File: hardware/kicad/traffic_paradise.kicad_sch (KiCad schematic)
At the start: 70 parts, among them J2 USB C, Q1 SS8050, Q2 SS8050, SW1 SW_Push, SW2 SW_Push, SW3 SW_Push, U1 ESP32-WROOM-32, U10 SN74LVC1G14DBVR, U11 SN74AHC125PWR, U2 AMS1117-3.3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

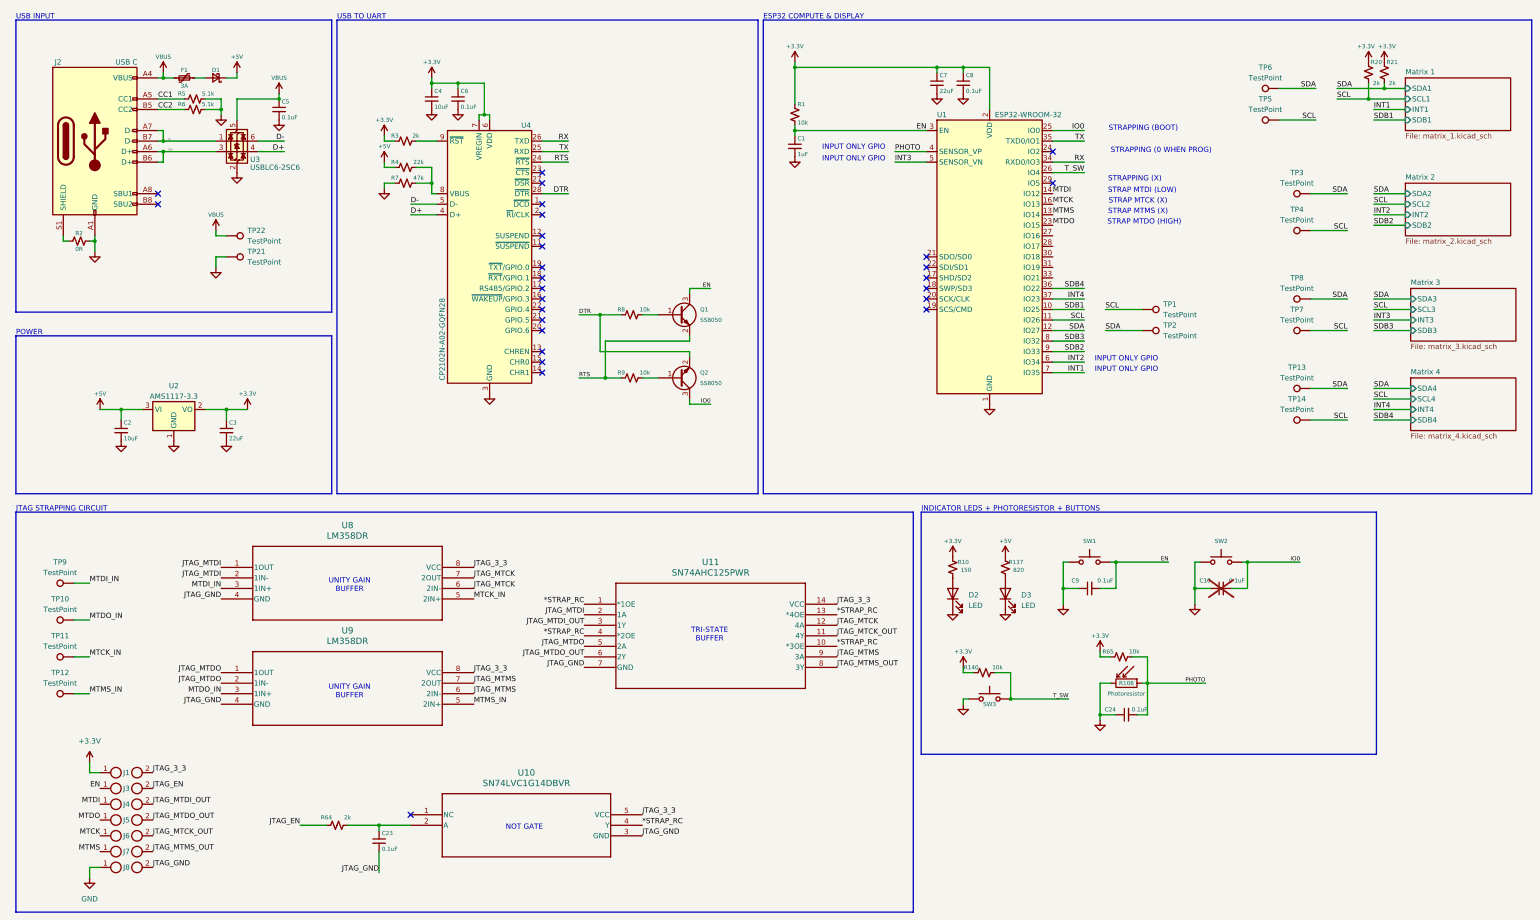
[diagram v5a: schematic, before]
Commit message: esp32c3 upgrade, route usb, fix errors
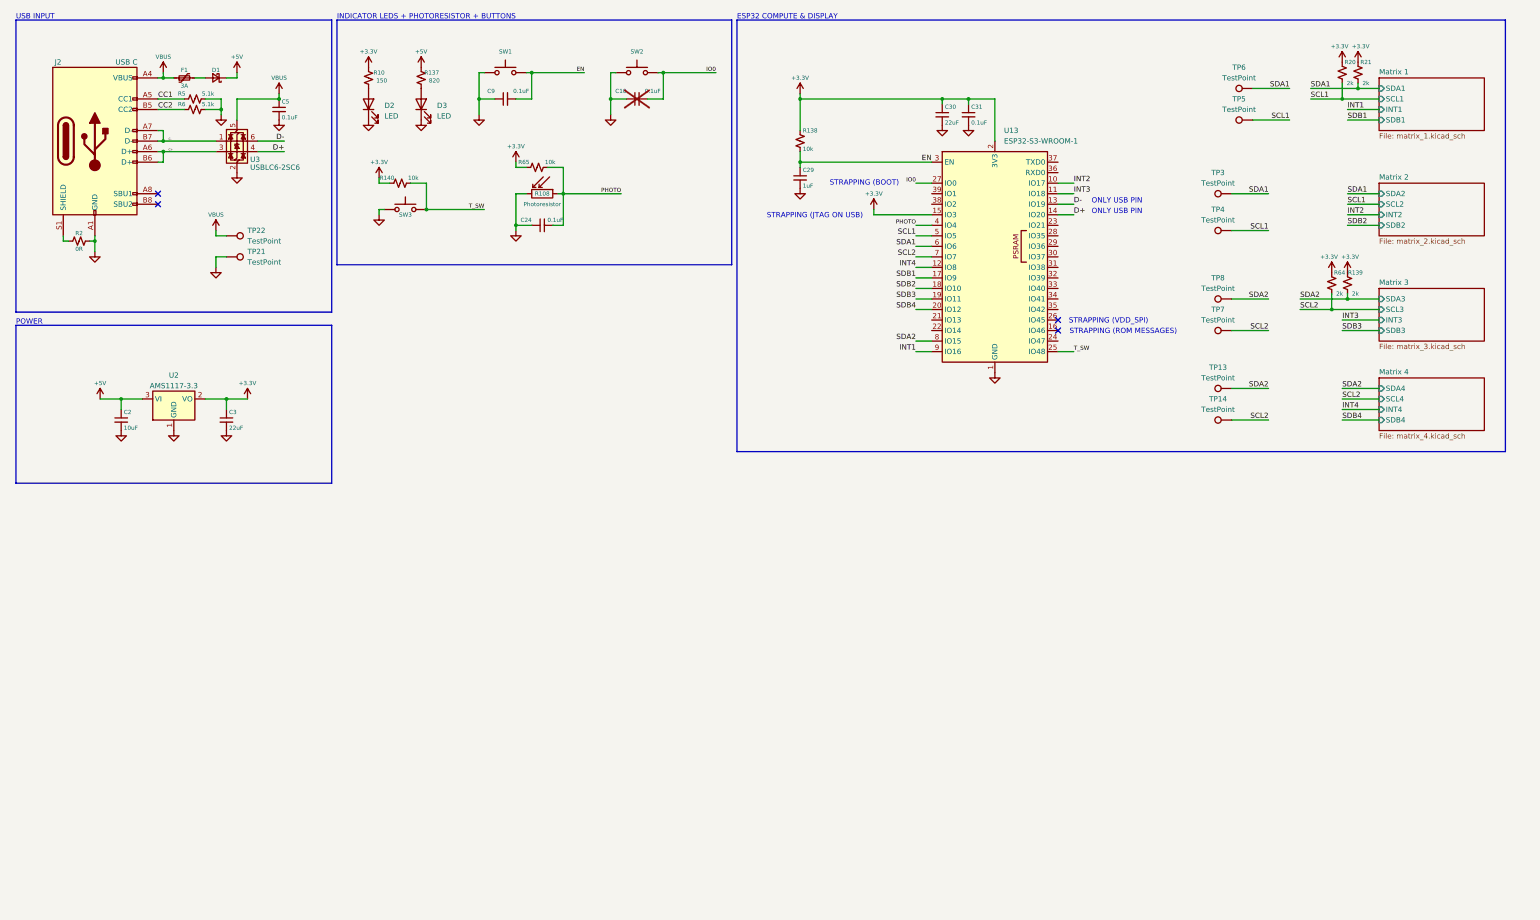
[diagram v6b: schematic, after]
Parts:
- removed C1: 1uF, Capacitor_SMD:C_0402_1005Metric, symbol Device:C_Small
- removed C23, C6, C8: 0.1uF, Capacitor_SMD:C_0402_1005Metric, symbol Device:C_Small
- removed C4: 10uF, Capacitor_SMD:C_0402_1005Metric, symbol Device:C_Small
- removed C7: 22uF, Capacitor_SMD:C_0603_1608Metric, symbol Device:C_Small
- removed J1, J3, J4, J5, J6, J7, J8: ~, Jumper:SolderJumper-2_P1.3mm_Open_TrianglePad1.0x1.5mm, symbol Isolators:breadboard_jumper
- removed Q1, Q2: SS8050, Package_TO_SOT_SMD:SOT-23, symbol Transistor_BJT:MMBT2222A
- removed R1, R8, R9: 10k, Resistor_SMD:R_0402_1005Metric, symbol Device:R_Small_US
- removed R3: 2k, Resistor_SMD:R_0402_1005Metric, symbol Device:R_Small_US
- removed R4: 22k, Resistor_SMD:R_0402_1005Metric, symbol Device:R_Small_US
- removed R7: 47k, Resistor_SMD:R_0402_1005Metric, symbol Device:R_Small_US
- removed TP1, TP10, TP11, TP12, TP2, TP9: TestPoint, TestPoint:TestPoint_Pad_D2.5mm, symbol Connector:TestPoint
- removed U1: ESP32-WROOM-32, RF_Module:ESP32-WROOM-32, symbol RF_Module:ESP32-WROOM-32
- removed U10: SN74LVC1G14DBVR, map_lbr:DBV5, symbol SN74LVC1G14DBVR:SN74LVC1G14DBVR
- removed U11: SN74AHC125PWR, map_lbr:PW14, symbol SN74AHC125PWR:SN74AHC125PWR
- removed U4: CP2102N-A02-GQFN28, Package_DFN_QFN:QFN-28-1EP_5x5mm_P0.5mm_EP3.35x3.35mm, symbol Interface_USB:CP2102N-Axx-xQFN28
- removed U8, U9: LM358DR, map_lbr:D8, symbol LM358DR:LM358DR
- added C29: 1uF, Capacitor_SMD:C_0402_1005Metric, symbol Device:C_Small
- added C30: 22uF, Capacitor_SMD:C_0603_1608Metric, symbol Device:C_Small
- added C31: 0.1uF, Capacitor_SMD:C_0402_1005Metric, symbol Device:C_Small
- added R138: 10k, Resistor_SMD:R_0402_1005Metric, symbol Device:R_Small_US
- added R139: 2k, Resistor_SMD:R_0402_1005Metric, symbol Device:R_Small_US
- added U13: ESP32-S3-WROOM-1, RF_Module:ESP32-S3-WROOM-1, symbol RF_Module:ESP32-S3-WROOM-1
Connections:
- net JTAG_EN is gone; now on net +3.3V: R64.1
- net +3.3V: now also C30.1, C31.1, R138.1, R139.1, U13.15 (IO3), U13.2 (3V3)
- net D+: now also U13.14 (IO20)
- net D-: now also U13.13 (IO19)
- net EN: now also C29.1, R138.2, U13.3 (EN)
- net GND: now also C29.2, C30.2, C31.2, U13.1 (GND), U13.40 (GND), U13.41 (GND)
- net INT1: now also U13.9 (IO16)
- net INT2: now also U13.10 (IO17)
- net INT3: now also U13.11 (IO18)
- net INT4: now also U13.12 (IO8)
- net IO0: now also U13.27 (IO0)
- net PHOTO: now also U13.4 (IO4)
- net SDB1: now also U13.17 (IO9)
- net SDB2: now also U13.18 (IO10)
- net SDB3: now also U13.19 (IO11)
- net SDB4: now also U13.20 (IO12)
- net T_SW: now also U13.25 (IO48)
- net SCL2: now reaches R64.2
- net SCL2: now also TP14.1, TP7.1, U13.7 (IO7)
- net SCL renamed SCL1
- net SCL1: now also U13.5 (IO5); no longer TP14.1, TP7.1
- net SDA renamed SDA1
- net SDA1: now also U13.6 (IO6); no longer TP13.1, TP8.1
- new net SDA2: R139.2, TP13.1, TP8.1, U13.8 (IO15)
- no-connect marks 27 -> 4
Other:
- note added: "ONLY USB PIN"
- note added: "STRAPPING (JTAG ON USB)"
- note added: "STRAPPING (ROM MESSAGES)"
- note added: "STRAPPING (VDD_SPI)"
- note removed: "INPUT ONLY GPIO"
- note removed: "JTAG STRAPPING CIRCUIT"
- note removed: "NOT GATE"
- note removed: "STRAP MTCK (X)"
- note removed: "STRAP MTDI (LOW)"
- note removed: "STRAP MTDO (HIGH)"
- note removed: "STRAP MTMS (X)"
- note removed: "STRAPPING (0 WHEN PROG)"
- note removed: "STRAPPING (X)"
- note removed: "TRI-STATE BUFFER"
- note removed: "UNITY GAIN BUFFER"
- note removed: "USB TO UART"
- moved on the sheet: C10, C2, C24, C3, C9, D2, D3, R10, R108, R137, R140, R20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

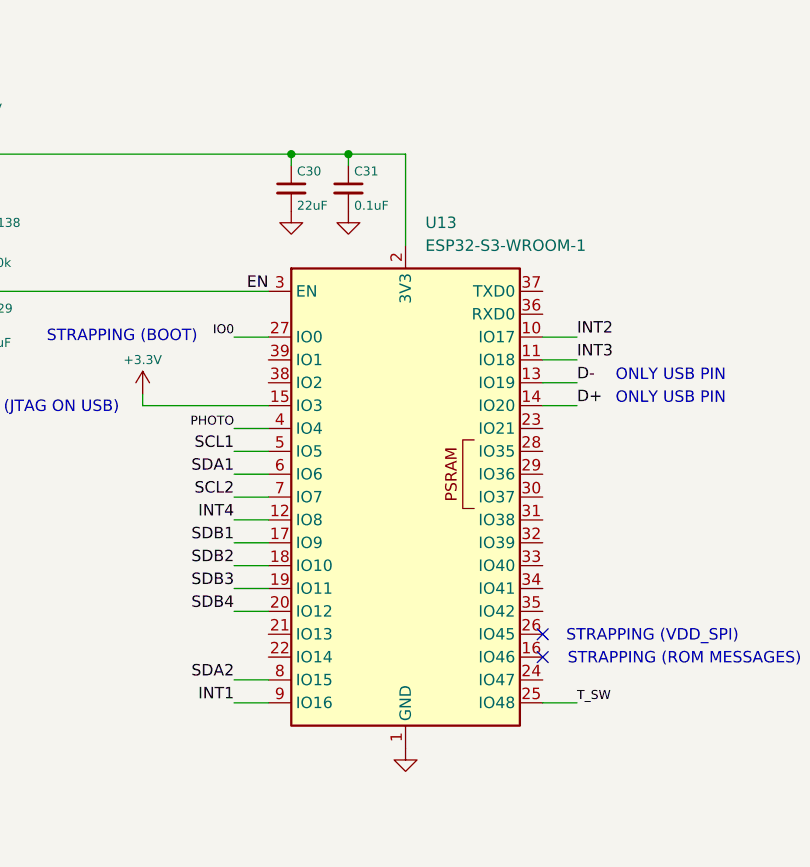
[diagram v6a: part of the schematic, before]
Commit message: Minor changes
Moved LED driver pins around and optimized board layout
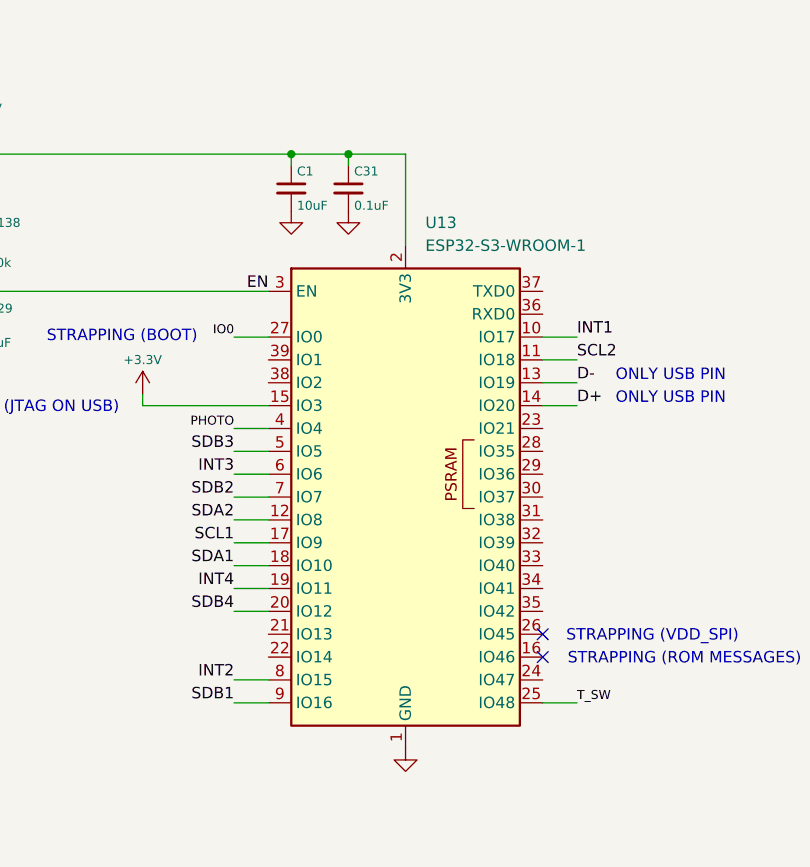
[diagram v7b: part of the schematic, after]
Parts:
- removed C30: 22uF, Capacitor_SMD:C_0603_1608Metric, symbol Device:C_Small
- added C1: 10uF, Capacitor_SMD:C_0402_1005Metric, symbol Device:C_Small
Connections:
- net +3.3V: now also C1.1
- net GND: now also C1.2
- net INT1: now also U13.10 (IO17); no longer U13.9 (IO16)
- net INT2: now also U13.8 (IO15); no longer U13.10 (IO17)
- net INT3: now also U13.6 (IO6); no longer U13.11 (IO18)
- net INT4: now also U13.19 (IO11); no longer U13.12 (IO8)
- net SCL1: now also U13.17 (IO9); no longer U13.5 (IO5)
- net SCL2: now also U13.11 (IO18); no longer U13.7 (IO7)
- net SDA1: now also U13.18 (IO10); no longer U13.6 (IO6)
- net SDA2: now also U13.12 (IO8); no longer U13.8 (IO15)
- net SDB1: now also U13.9 (IO16); no longer U13.17 (IO9)
- net SDB2: now also U13.7 (IO7); no longer U13.18 (IO10)
- net SDB3: now also U13.5 (IO5); no longer U13.19 (IO11)
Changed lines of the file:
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@@
 	(wire
 		(pts
-			(xy 242.57 105.41) (xy 246.38 105.41)
+			(xy 280.67 64.77) (xy 276.86 64.77)
 		)
 		(stroke
@@
 	(wire
 		(pts
-			(xy 242.57 85.09) (xy 246.38 85.09)
+			(xy 242.57 92.71) (xy 246.38 92.71)
 		)
 		(stroke
@@
 	(wire
 		(pts
-			(xy 242.57 102.87) (xy 246.38 102.87)
+			(xy 242.57 85.09) (xy 246.38 85.09)
 		)
 		(stroke
@@
 	(wire
 		(pts
-			(xy 276.86 67.31) (xy 280.67 67.31)
+			(xy 246.38 80.01) (xy 242.57 80.01)
 		)
 		(stroke
@@
 	(wire
 		(pts
-			(xy 242.57 87.63) (xy 246.38 87.63)
+			(xy 242.57 105.41) (xy 246.38 105.41)
 		)
 		(stroke
@@
 	(wire
 		(pts
-			(xy 242.57 82.55) (xy 246.38 82.55)
+			(xy 280.67 67.31) (xy 276.86 67.31)
 		)
 		(stroke
@@
 	(wire
 		(pts
-			(xy 242.57 80.01) (xy 246.38 80.01)
+			(xy 242.57 90.17) (xy 246.38 90.17)
 		)
 		(stroke
@@
 	(wire
 		(pts
-			(xy 242.57 77.47) (xy 246.38 77.47)
+			(xy 242.57 87.63) (xy 246.38 87.63)
 		)
 		(stroke
@@
 	(wire
 		(pts
-			(xy 242.57 92.71) (xy 246.38 92.71)
+			(xy 242.57 77.47) (xy 246.38 77.47)
 		)
 		(stroke
@@
 	(wire
 		(pts
-			(xy 242.57 90.17) (xy 246.38 90.17)
+			(xy 242.57 82.55) (xy 246.38 82.55)
 		)
 		(stroke
@@
 	(wire
 		(pts
-			(xy 276.86 64.77) (xy 280.67 64.77)
+			(xy 242.57 102.87) (xy 246.38 102.87)
 		)
 		(stroke
@@
 	)
 	(label "SDB3"
-		(at 242.57 92.71 180)
+		(at 242.57 77.47 180)
 		(fields_autoplaced yes)
 		(effects
@@
 	)
 	(label "SDA1"
-		(at 242.57 80.01 180)
+		(at 242.57 90.17 180)
 		(fields_autoplaced yes)
 		(effects
@@
 	)
 	(label "SCL2"
-		(at 242.57 82.55 180)
+		(at 280.67 67.31 0)
 		(fields_autoplaced yes)
 		(effects
@@
 				(size 1.27 1.27)
 			)
-			(justify right bottom)
+			(justify left bottom)
 		)
 	)
@@
 	)
 	(label "INT3"
-		(at 280.67 67.31 0)
+		(at 242.57 80.01 180)
 		(fields_autoplaced yes)
 		(effects
@@
 				(size 1.27 1.27)
 			)
-			(justify left bottom)
+			(justify right bottom)
 		)
 	)
@@
 	)
 	(label "INT2"
-		(at 280.67 64.77 0)
+		(at 242.57 102.87 180)
 		(fields_autoplaced yes)
 		(effects
@@
 				(size 1.27 1.27)
 			)
-			(justify left bottom)
+			(justify right bottom)
 		)
 	)
@@
 	)
 	(label "INT4"
-		(at 242.57 85.09 180)
+		(at 242.57 92.71 180)
 		(fields_autoplaced yes)
 		(effects
@@
 	)
 	(label "SDB2"
-		(at 242.57 90.17 180)
+		(at 242.57 82.55 180)
 		(fields_autoplaced yes)
 		(effects
@@
 	)
 	(label "INT1"
-		(at 242.57 105.41 180)
+		(at 280.67 64.77 0)
 		(fields_autoplaced yes)
 		(effects
@@
 				(size 1.27 1.27)
 			)
-			(justify right bottom)
+			(justify left bottom)
 		)
 	)
@@
 	)
 	(label "SDB1"
-		(at 242.57 87.63 180)
+		(at 242.57 105.41 180)
 		(fields_autoplaced yes)
 		(effects
@@
 	)
 	(label "SCL1"
-		(at 242.57 77.47 180)
+		(at 242.57 87.63 180)
 		(fields_autoplaced yes)
 		(effects
@@
 	)
 	(label "SDA2"
-		(at 242.57 102.87 180)
+		(at 242.57 85.09 180)
 		(fields_autoplaced yes)
 		(effects
@@
 	)
 	(symbol
+		(lib_id "Device:C_Small")
+		(at 248.92 48.26 0)
+		(unit 1)
+		(exclude_from_sim no)
+		(in_bom yes)
+		(on_board yes)
+		(dnp no)
+		(property "Reference" "C1"
+			(at 249.555 46.355 0)
+			(effects
+				(font
+					(size 1 1)
+				)
+				(justify left)
+			)
+		)
+		(property "Value" "10uF"
+			(at 249.555 50.165 0)
+			(effects
+				(font
+					(size 1 1)
+				)
+				(justify left)
+			)
+		)
+		(property "Footprint" "Capacitor_SMD:C_0402_1005Metric"
+			(at 248.92 48.26 0)
+			(effects
+				(font
+					(size 1.27 1.27)
+				)
+				(hide yes)
+			)
+		)
+		(property "Datasheet" "~"
+			(at 248.92 48.26 0)
+			(effects
+				(font
+					(size 1.27 1.27)
+				)
+				(hide yes)
+			)
+		)
+		(property "Description" "Unpolarized capacitor, small symbol"
+			(at 248.92 48.26 0)
+			(effects
+				(font
+					(size 1.27 1.27)
+				)
+				(hide yes)
+			)
+		)
+		(pin "2"
+		)
+		(pin "1"
+		)
+		(instances
+			(project "traffic_paradise"
+				(path "/911505fc-874d-4338-908e-12054bdd5112"
+					(reference "C1")
+					(unit 1)
+				)
+			)
+		)
+	)
+	(symbol
 		(lib_id "Device:R_Small_US")
 		(at 345.44 38.1 0)
@@
 					(unit 1)
 				)
-			)
-		)
-	)
-	(symbol
-		(lib_id "Device:C_Small")
-		(at 248.92 48.26 0)
-		(unit 1)
-		(exclude_from_sim no)
-		(in_bom yes)
-		(on_board yes)
-		(dnp no)
-		(property "Reference" "C30"
-			(at 249.555 46.355 0)
-			(effects
-				(font
-					(size 1 1)
-				)
-				(justify left)
-			)
-		)
-		(property "Value" "22uF"
-			(at 249.555 50.165 0)
-			(effects
-				(font
-					(size 1 1)
-				)
-				(justify left)
-			)
-		)
-		(property "Footprint" "Capacitor_SMD:C_0603_1608Metric"
-			(at 248.92 48.26 0)
-			(effects
-				(font
-					(size 1.27 1.27)
-				)
-				(hide yes)
-			)
-		)
-		(property "Datasheet" "~"
-			(at 248.92 48.26 0)
-			(effects
-				(font
-					(size 1.27 1.27)
-				)
-				(hide yes)
-			)
-		)
-		(property "Description" "Unpolarized capacitor, small symbol"
-			(at 248.92 48.26 0)
-			(effects
-				(font
-					(size 1.27 1.27)
-				)
-				(hide yes)
-			)
-		)
-		(pin "2"
-		)
-		(pin "1"
-		)
-		(instances
-			(project "traffic_paradise"
-				(path "/911505fc-874d-4338-908e-12054bdd5112"
-					(reference "C30")
-					(unit 1)
-				)

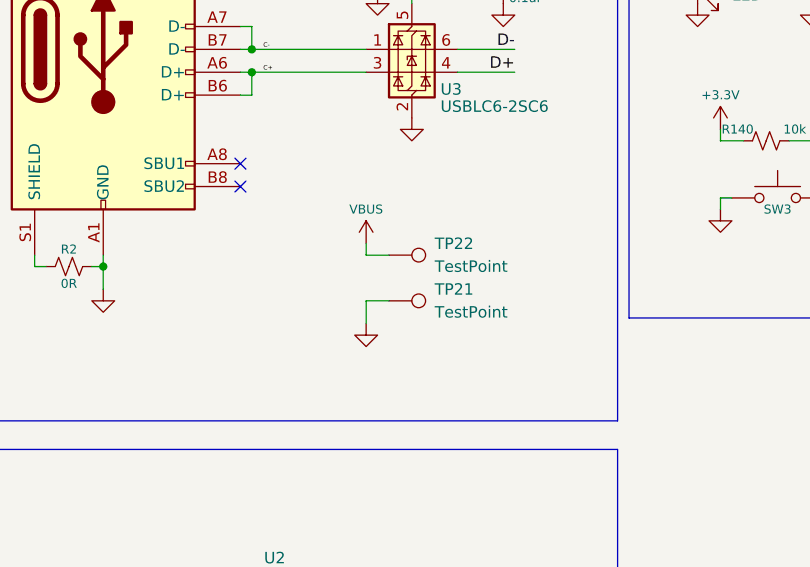
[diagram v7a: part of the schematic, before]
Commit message: add reverse current protection on wall mount & generate BOM
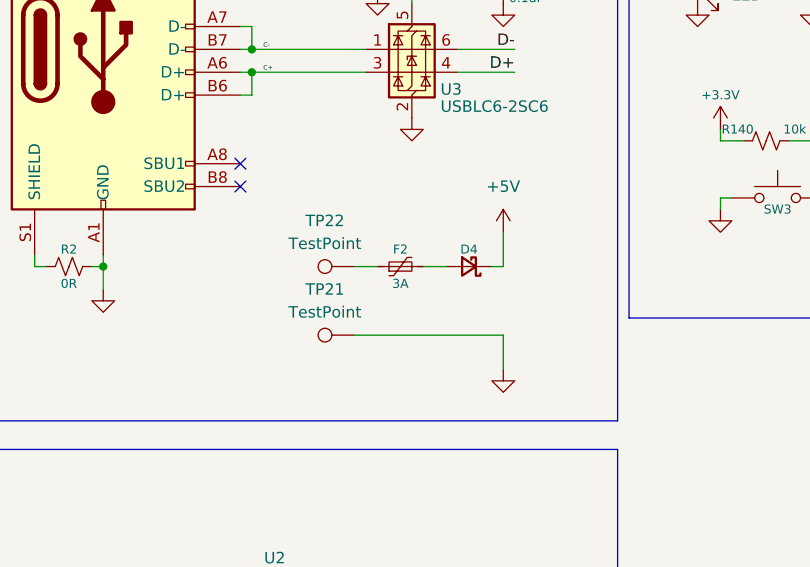
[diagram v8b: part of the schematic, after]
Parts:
- added D4: Schottky, Diode_SMD:D_SMA, symbol Device:D_Schottky_Small
- added F2: 3A, Fuse:Fuse_1206_3216Metric, symbol Device:Polyfuse_Small
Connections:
- net +5V: now also D4.1 (K)
- net VBUS: no longer TP22.1
- new net: F2.1, TP22.1
- new net: D4.2 (A), F2.2
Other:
- moved on the sheet: TP21, TP22
